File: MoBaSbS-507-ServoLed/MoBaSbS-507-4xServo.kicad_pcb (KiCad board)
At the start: 2 copper layers, 40.6 x 81.3 mm, 36 parts, among them J1 Conn_02x05_Counter_Clockwise, J2 Conn_02x06_Odd_Even, J5 Conn_02x05_Counter_Clockwise, P1 2x5_Buchse, P3 PSS-3G, P4 PSS-3G, P5 2x5_Buchse, U1 PCA9685PW

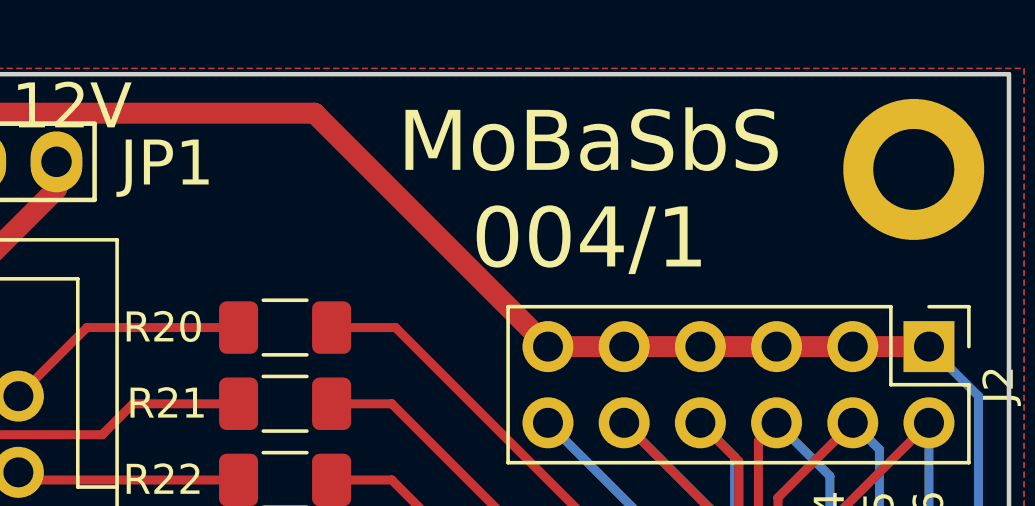
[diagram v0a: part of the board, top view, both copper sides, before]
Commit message: Finished up PCBs, added stencil
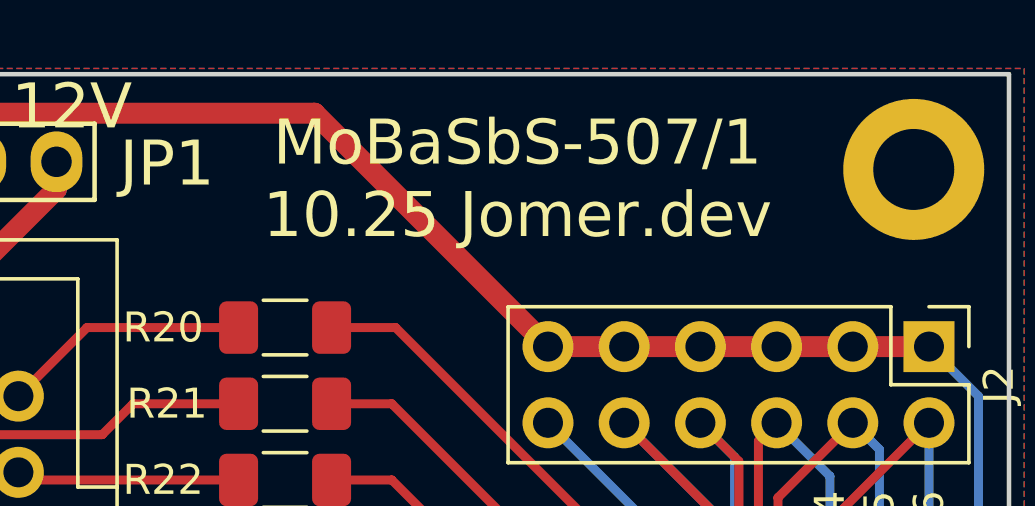
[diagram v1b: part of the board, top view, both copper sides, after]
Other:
- board text added: "MoBaSbS-507/1 10.25 Jomer.dev"
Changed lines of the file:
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@@
-		)
-	)
-	(gr_text "MoBaSbS\n004/1"
-		(at 115.316 88.3285 0)
-		(layer "F.SilkS")
-		(effects
-			(font
-				(size 2 2)
-				(thickness 0.3)
-			)
 		)
 	)
@@
 		(layer "F.SilkS")
 		(effects
+			(font
+				(size 1.5 1.5)
+				(thickness 0.3)
+			)
+		)
+	)
+	(gr_text "MoBaSbS-507/1\n10.25 Jomer.dev"
+		(at 112.903 87.9475 0)
+		(layer "F.SilkS")
+		(effects
